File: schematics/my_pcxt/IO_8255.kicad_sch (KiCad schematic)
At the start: 1 part, among them U11 82C55A

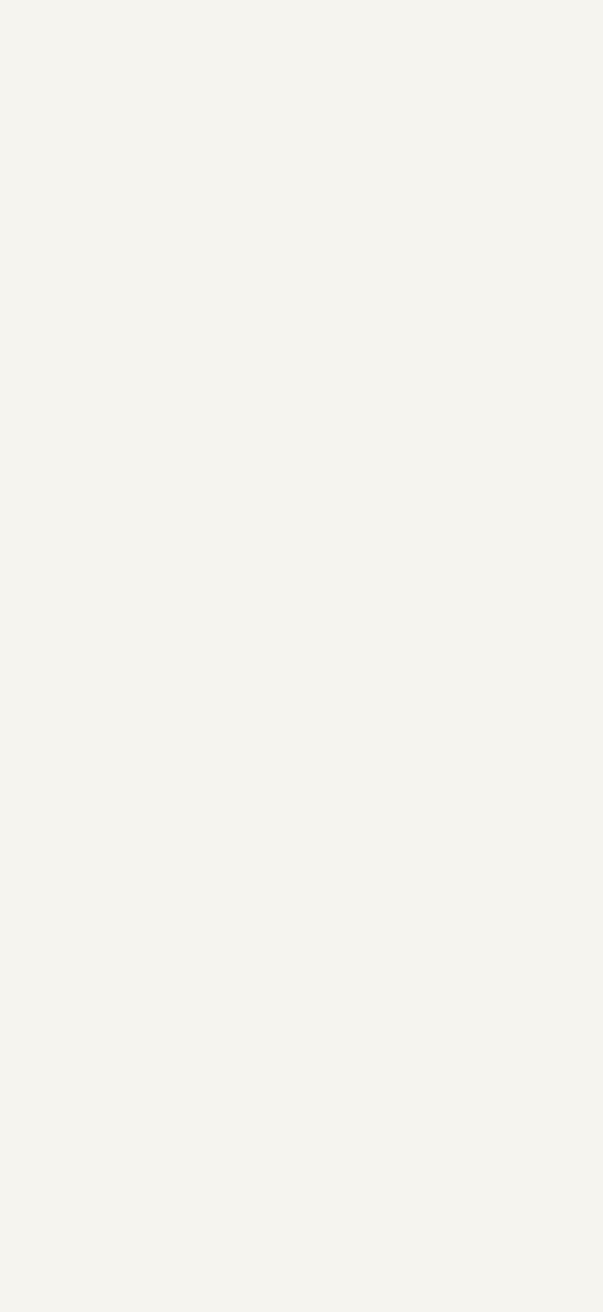
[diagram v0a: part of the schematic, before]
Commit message: Implemented 8259 e 8253
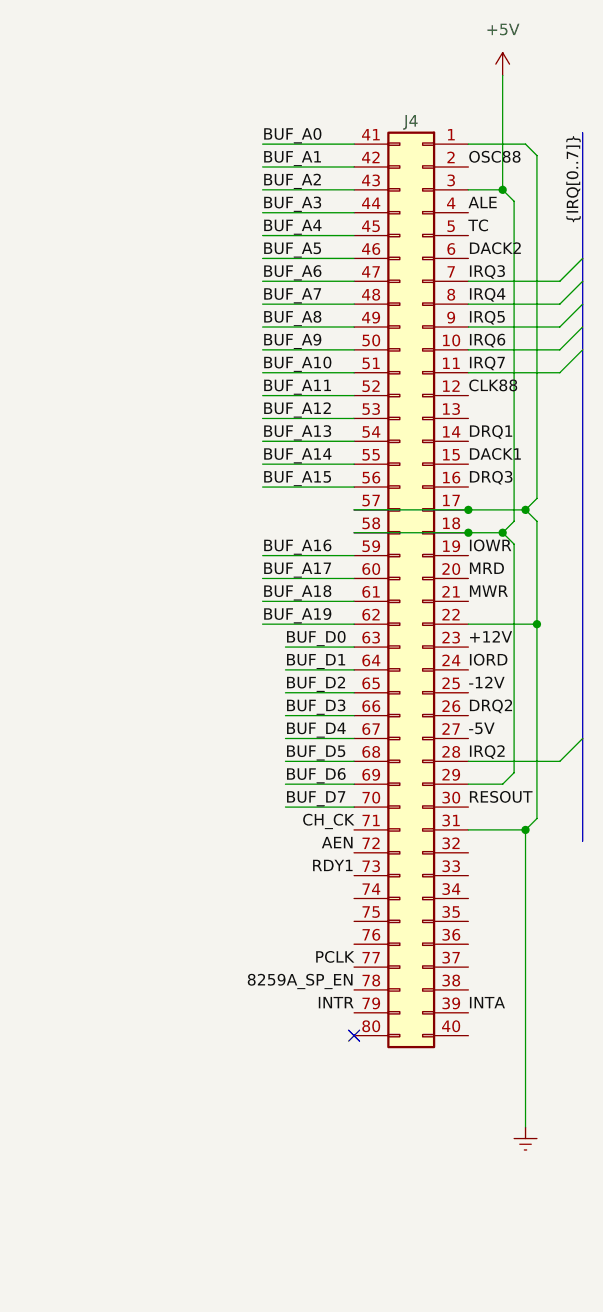
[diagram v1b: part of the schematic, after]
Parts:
- added J4: Conn_02x40_Top_Bottom, symbol Connector_Generic:Conn_02x40_Top_Bottom
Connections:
- net +5V: now also J4.18 (Pin_18), J4.29 (Pin_29), J4.3 (Pin_3), J4.58 (Pin_58)
- net BUF_A0: now also J4.41 (Pin_41)
- net BUF_A1: now also J4.42 (Pin_42)
- net BUF_D0: now also J4.63 (Pin_63)
- net BUF_D1: now also J4.64 (Pin_64)
- net BUF_D2: now also J4.65 (Pin_65)
- net BUF_D3: now also J4.66 (Pin_66)
- net BUF_D4: now also J4.67 (Pin_67)
- net BUF_D5: now also J4.68 (Pin_68)
- net BUF_D6: now also J4.69 (Pin_69)
- net BUF_D7: now also J4.70 (Pin_70)
- new net +12V: J4.23 (Pin_23)
- new net -12V: J4.25 (Pin_25)
- new net -5V: J4.27 (Pin_27)
- new net 8259A_SP_EN: J4.78 (Pin_78)
- new net AEN: J4.72 (Pin_72)
- new net ALE: J4.4 (Pin_4)
- new net BUF_A10: J4.51 (Pin_51)
- new net BUF_A11: J4.52 (Pin_52)
- new net BUF_A12: J4.53 (Pin_53)
- new net BUF_A13: J4.54 (Pin_54)
- new net BUF_A14: J4.55 (Pin_55)
- new net BUF_A15: J4.56 (Pin_56)
- new net BUF_A16: J4.59 (Pin_59)
- new net BUF_A17: J4.60 (Pin_60)
- new net BUF_A18: J4.61 (Pin_61)
- new net BUF_A19: J4.62 (Pin_62)
- new net BUF_A2: J4.43 (Pin_43)
- new net BUF_A3: J4.44 (Pin_44)
- new net BUF_A4: J4.45 (Pin_45)
- new net BUF_A5: J4.46 (Pin_46)
- new net BUF_A6: J4.47 (Pin_47)
- new net BUF_A7: J4.48 (Pin_48)
- new net BUF_A8: J4.49 (Pin_49)
- new net BUF_A9: J4.50 (Pin_50)
- new net CH_CK: J4.71 (Pin_71)
- new net CLK88: J4.12 (Pin_12)
- new net DACK1: J4.15 (Pin_15)
- new net DACK2: J4.6 (Pin_6)
- new net DRQ1: J4.14 (Pin_14)
- new net DRQ2: J4.26 (Pin_26)
- new net DRQ3: J4.16 (Pin_16)
- new net GNDREF: J4.1 (Pin_1), J4.17 (Pin_17), J4.22 (Pin_22), J4.31 (Pin_31), J4.57 (Pin_57)
- new net INTA: J4.39 (Pin_39)
- new net INTR: J4.79 (Pin_79)
- new net IORD: J4.24 (Pin_24)
- new net IOWR: J4.19 (Pin_19)
- new net IRQ2: J4.28 (Pin_28)
- new net IRQ3: J4.7 (Pin_7)
- new net IRQ4: J4.8 (Pin_8)
- new net IRQ5: J4.9 (Pin_9)
- new net IRQ6: J4.10 (Pin_10)
- new net IRQ7: J4.11 (Pin_11)
- new net MRD: J4.20 (Pin_20)
- new net MWR: J4.21 (Pin_21)
- new net OSC88: J4.2 (Pin_2)
- new net PCLK: J4.77 (Pin_77)
- new net RDY1: J4.73 (Pin_73)
- new net RESOUT: J4.30 (Pin_30)
- new net TC: J4.5 (Pin_5)
- no-connect marks 9 -> 10

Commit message: Updating schematics
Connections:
- net 8255_CS: now also J4.76 (Pin_76)
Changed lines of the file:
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@@
+    (effects (font (size 1.27 1.27)) (justify right bottom))
+  )
+  (label "8255_CS" (at 240.03 119.38 180) (fields_autoplaced)
     (effects (font (size 1.27 1.27)) (justify right bottom))
   )

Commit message: Updating code...
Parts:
- added C23: 430nF, symbol Device:C
- added J7: Speaker, symbol Connector_Generic:Conn_01x02
- added Q2: 2N3904, Package_TO_SOT_THT:TO-92_Inline, symbol Transistor_BJT:2N3904
- added R10: 33R, symbol Device:R
- added U25: 74LS08, symbol 74xx:74LS08
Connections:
- net +5V: now also J7.1 (Pin_1)
- net BUF_D0: no longer U11.34 (D0)
- net BUF_D1: no longer U11.33 (D1)
- net BUF_D2: no longer U11.32 (D2)
- net BUF_D3: no longer U11.31 (D3)
- net BUF_D4: no longer U11.30 (D4)
- net BUF_D5: no longer U11.29 (D5)
- net BUF_D6: no longer U11.28 (D6)
- net BUF_D7: no longer U11.27 (D7)
- net GNDREF: now also C23.2, Q2.1 (E)
- net timer2GateSpeaker: now reaches U11.18 (PB0)
- net at U11.19 (PB1): now also U25.2
- net ICH_ACK: no longer names the net of U11.11 (PC6)
- net ICH_D0: no longer names the net of U11.4 (PA0)
- net ICH_D1: no longer names the net of U11.3 (PA1)
- net ICH_D2: no longer names the net of U11.2 (PA2)
- net ICH_D3: no longer names the net of U11.1 (PA3)
- net ICH_D4: no longer names the net of U11.40 (PA4)
- net ICH_D5: no longer names the net of U11.39 (PA5)
- net ICH_D6: no longer names the net of U11.38 (PA6)
- net ICH_D7: no longer names the net of U11.37 (PA7)
- net ICH_IBF: no longer names the net of U11.12 (PC5)
- net ICH_OBF: no longer names the net of U11.10 (PC7)
- net ICH_STB: no longer names the net of U11.13 (PC4)
- net LED_GREEN: no longer names the net of U11.14 (PC0)
- net LED_RED: no longer names the net of U11.16 (PC2)
- net LED_YELLOW: no longer names the net of U11.15 (PC1)
- new net: C23.1, Q2.3 (C), R10.1
- new net: Q2.2 (B), U25.3
- new net: J7.2 (Pin_2), R10.2
- new net D0: U11.34 (D0)
- new net D1: U11.33 (D1)
- new net D2: U11.32 (D2)
- new net D3: U11.31 (D3)
- new net D4: U11.30 (D4)
- new net D5: U11.29 (D5)
- new net D6: U11.28 (D6)
- new net D7: U11.27 (D7)
- new net SPEAKER_DATA: U25.1
- no-connect marks 10 -> 1
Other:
- moved on the sheet: U11
